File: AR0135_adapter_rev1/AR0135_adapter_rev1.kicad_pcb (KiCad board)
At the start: 2 copper layers, 60 x 40 mm, 10 parts, among them J1 Conn_01x30, J2 DF 12-36-DP, J3 Conn_01x08, J4 Conn_01x08, J5 Conn_01x08, J6 Conn_01x02

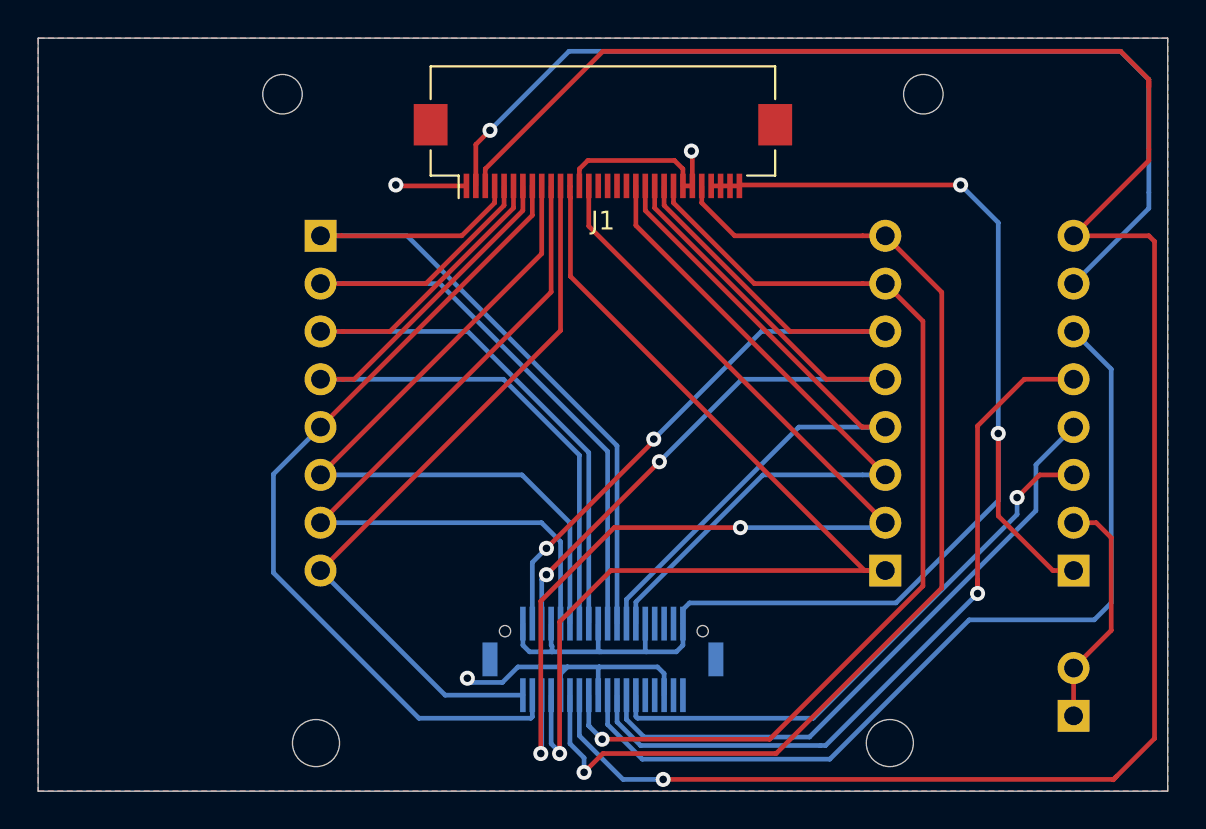
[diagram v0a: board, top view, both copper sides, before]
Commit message: Appiko logo added on Silk screen
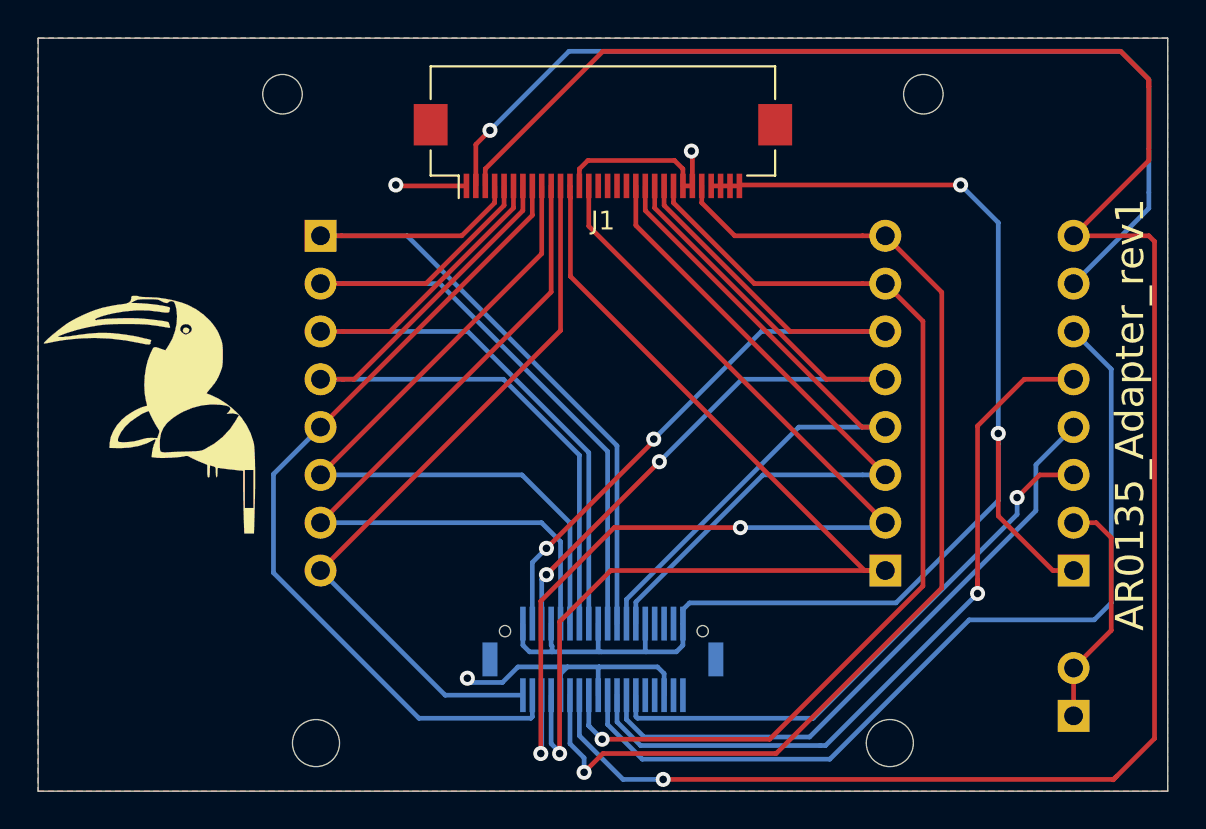
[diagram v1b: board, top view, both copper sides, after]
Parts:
- added G***: Appiko_LOGO_img, sense:Appiko_LOGO_img, F.Cu at (15.9, 30.0)
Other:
- board text added: "AR0135_Adapter_rev1"
